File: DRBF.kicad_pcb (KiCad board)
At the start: 2 copper layers, 80 x 100 mm, 94 parts, among them J1 VER-A, J10 INV-A, J11 INV-B, J2 In-A, J3 In-AB, J4 In-B, J5 Eurorack_Power, J6 VER-B, J7 Out-A, J8 Out-AB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

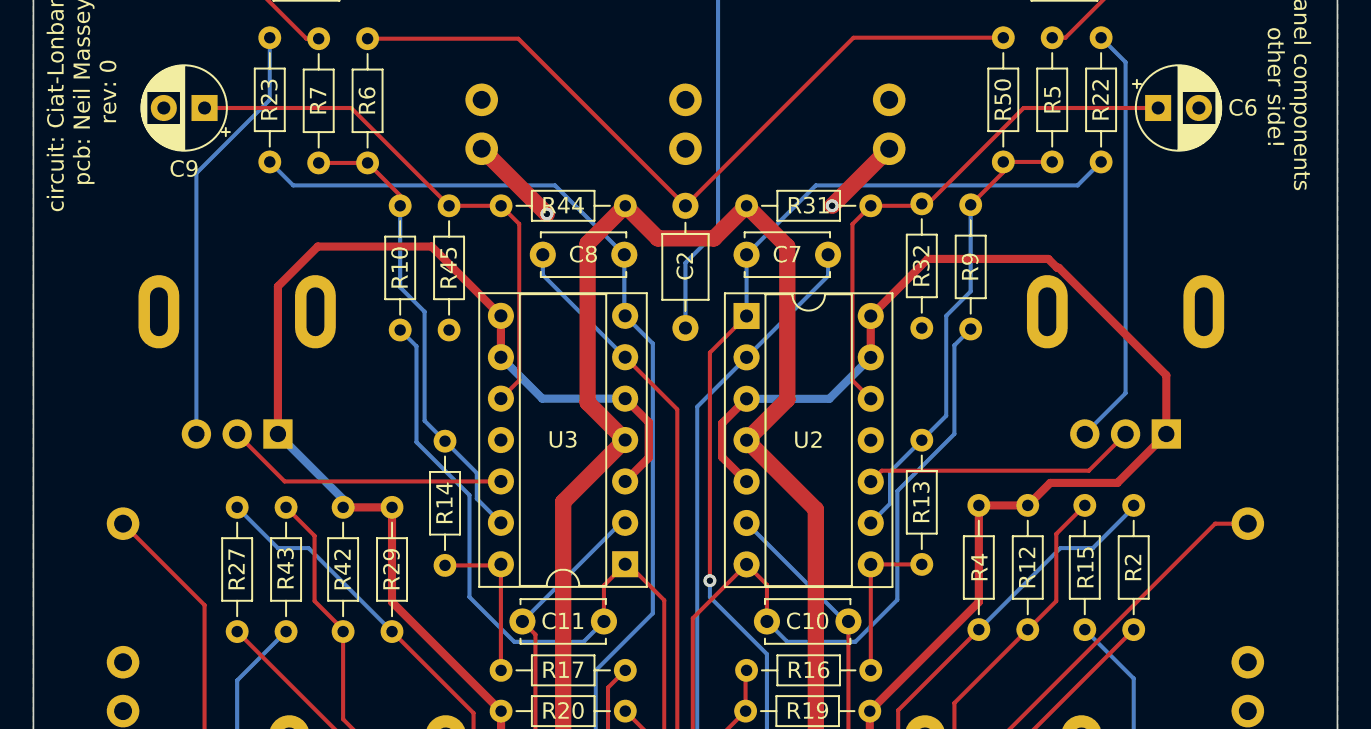
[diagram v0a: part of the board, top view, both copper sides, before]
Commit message: Added negative voltage protection diodes
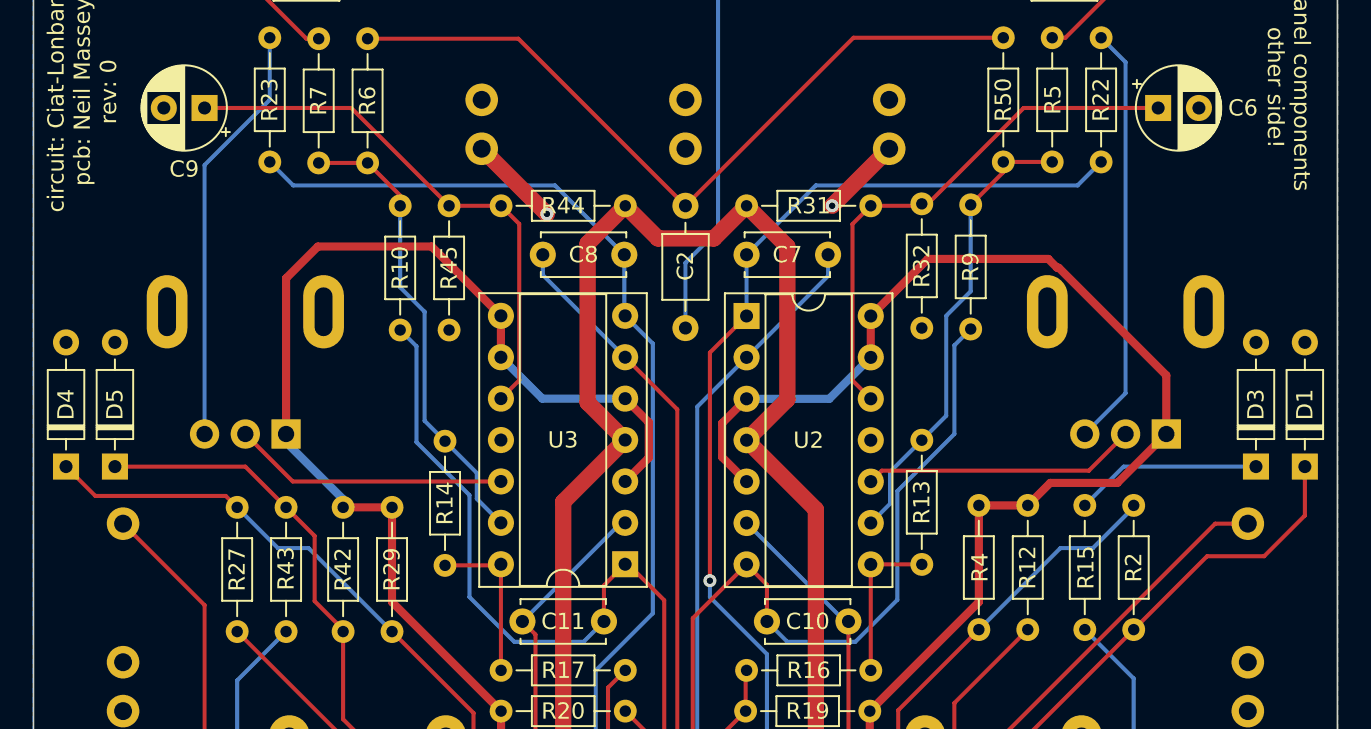
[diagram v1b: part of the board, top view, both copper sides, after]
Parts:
- added D1: BAT42, Diode_THT:D_DO-35_SOD27_P7.62mm_Horizontal, F.Cu at (78.0, 32.5)
- added D3: BAT42, Diode_THT:D_DO-35_SOD27_P7.62mm_Horizontal, F.Cu at (75.0, 32.5)
- added D4: BAT42, Diode_THT:D_DO-35_SOD27_P7.62mm_Horizontal, F.Cu at (2.00, 32.5)
- added D5: BAT42, Diode_THT:D_DO-35_SOD27_P7.62mm_Horizontal, F.Cu at (5.00, 32.5)
- moved RV4 0.50 mm to (13.0, 23.0)
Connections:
- R15 pad 1: Net-(Q4-Pad2) -> Net-(R15-Pad1)
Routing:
- net Net-(RV2-Pad2): track 18.3 -> 34.7 mm
- net Net-(Q8-Pad2): track 32.0 -> 43.5 mm
- net Net-(Q6-Pad2): track 41.7 -> 53.2 mm
- net Net-(R15-Pad1): track 0.00 -> 11.5 mm
- net Net-(Q4-Pad2): track 32.2 -> 23.1 mm
- net Net-(RV4-Pad2): track 17.4 -> 16.9 mm
